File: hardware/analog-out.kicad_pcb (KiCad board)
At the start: 2 copper layers, 30 x 35 mm, 30 parts, among them P1 CON-SENSOR, P2 CONN_5, U1 M24C64, U2 MCP4725A0, U3 TLV272IS, U4 DRILL, U5 DRILL, U6 DRILL, U7 DRILL

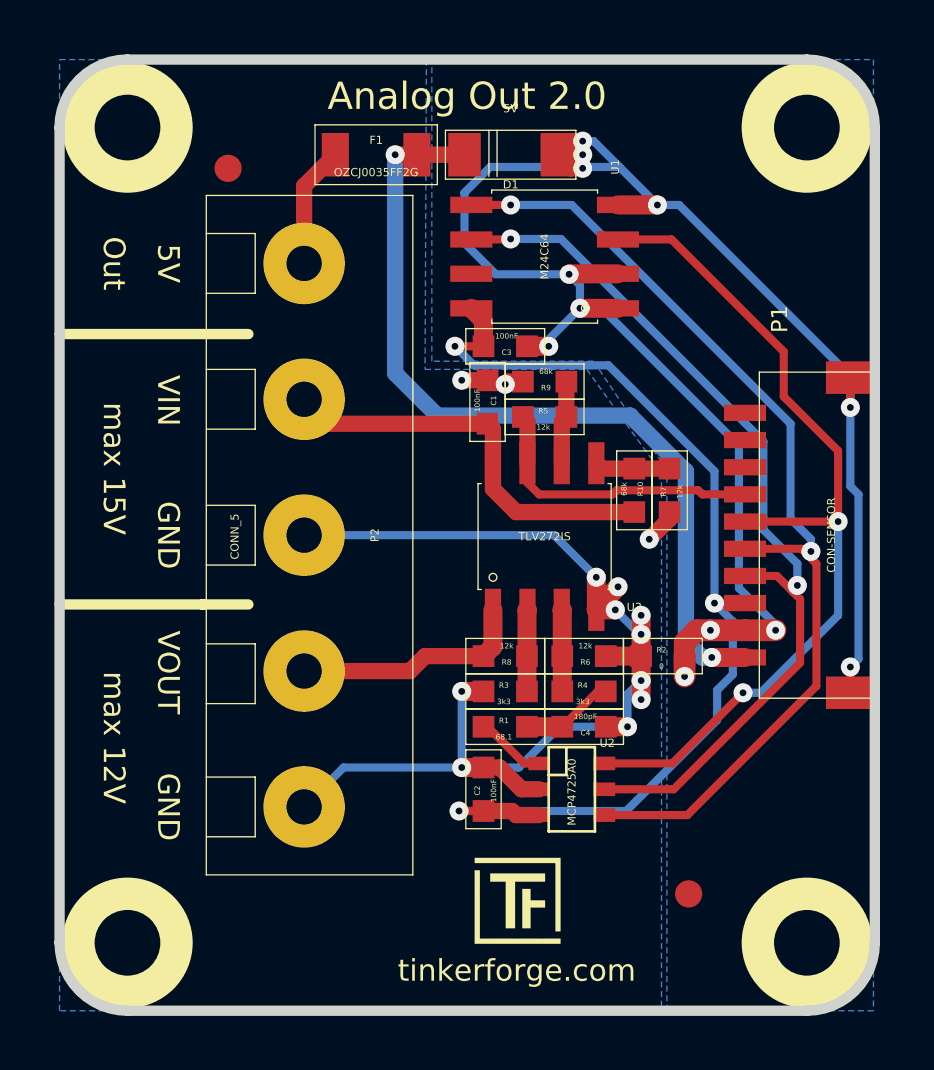
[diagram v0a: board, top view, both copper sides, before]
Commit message: use tinkerforge symbols instead of kicad symbols
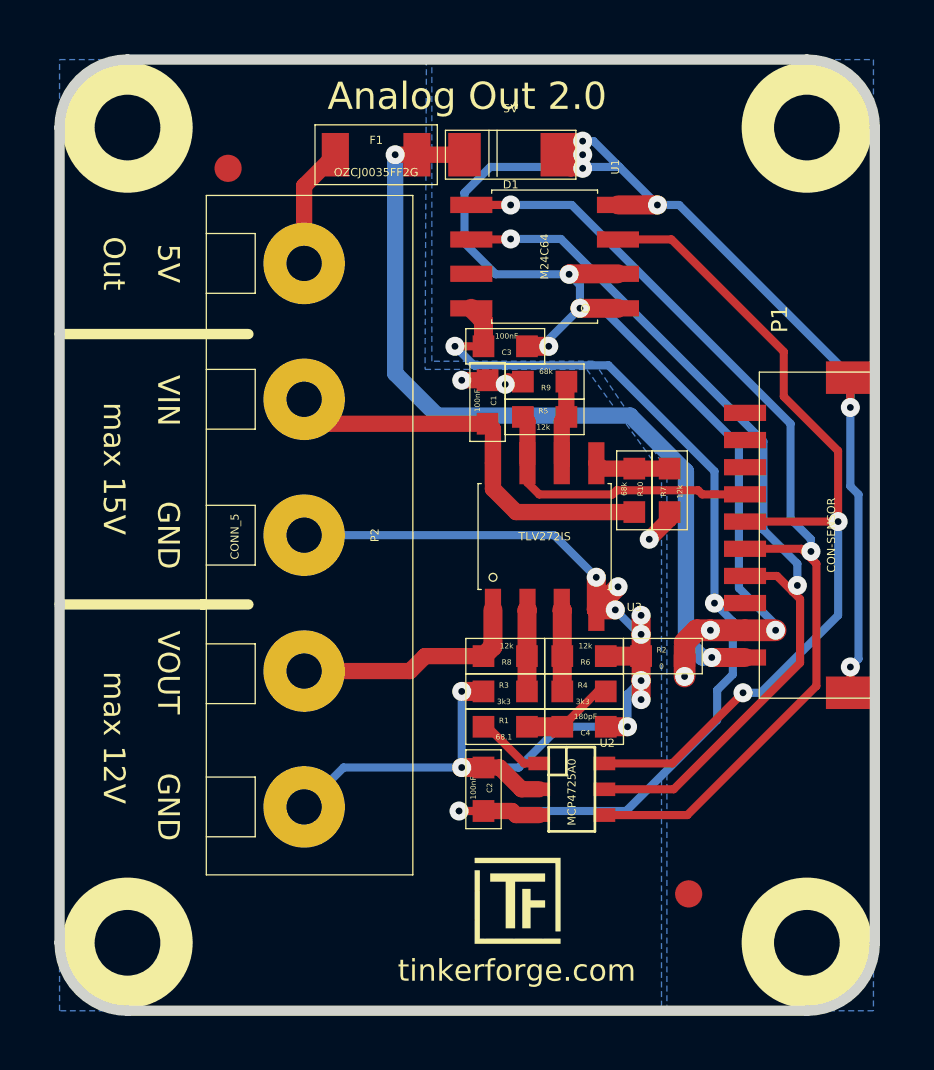
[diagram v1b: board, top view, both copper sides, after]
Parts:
- turned C2 to 90 degrees
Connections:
- C2 pad 1: AGND -> 3V3
- C2 pad 2: 3V3 -> AGND
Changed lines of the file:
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@@
-(kicad_pcb (version 4) (host pcbnew "(2015-03-18 BZR 5525)-product")
+(kicad_pcb (version 4) (host pcbnew 4.0.7-e0-6372~58~ubuntu16.10.1)
   (general
     (links 50)
     (no_connects 0)
-    (area 137.195139 81.720139 281.746642 165.290183)
+    (area 137.858499 82.381719 168.240721 117.765501)
     (thickness 1.6002)
     (drawings 22)
@@
   )
   (module kicad-libraries:0603 (layer Vorderseite)
-    (at 153.65 109.425 270)
+    (at 153.65 109.425 90)
     (attr smd)
-    (fp_text reference C2 (at 0.05 0.225 270) (layer F.SilkS)
+    (fp_text reference C2 (at 0.05 0.225 90) (layer F.SilkS)
       (effects (font (size 0.2 0.2) (thickness 0.05)))
     )
-    (fp_text value 100nF (at 0.05 -0.375 270) (layer F.SilkS)
+    (fp_text value 100nF (at 0.05 -0.375 90) (layer F.SilkS)
       (effects (font (size 0.2 0.2) (thickness 0.05)))
     )
@@
     (fp_line (start 1.45034 0.65024) (end -1.45034 0.65024) (layer F.SilkS) (width 0.001))
     (fp_line (start -1.45034 0.65024) (end -1.45034 -0.65024) (layer F.SilkS) (width 0.001))
-    (pad 1 smd rect (at -0.8001 0 270) (size 0.8001 0.8001) (layers Vorderseite F.Paste F.Mask)
-      (net 6 AGND))
-    (pad 2 smd rect (at 0.8001 0 270) (size 0.8001 0.8001) (layers Vorderseite F.Paste F.Mask)
+    (pad 1 smd rect (at -0.8001 0 90) (size 0.8001 0.8001) (layers Vorderseite F.Paste F.Mask)
       (net 7 3V3))
+    (pad 2 smd rect (at 0.8001 0 90) (size 0.8001 0.8001) (layers Vorderseite F.Paste F.Mask)
+      (net 6 AGND))
   )
   (module kicad-libraries:0603 (layer Vorderseite)
@@
   (via (at 157.3 86.575) (size 0.70104) (layers Vorderseite Rückseite) (net 2))
   (segment (start 156.34926 86.075) (end 156.84926 85.575) (width 0.59944) (layer Vorderseite) (net 2))
+  (segment (start 153.9 86.525) (end 157.3 86.525) (width 0.29972) (layer Rückseite) (net 2))
+  (segment (start 157.3 86.525) (end 158.65 86.525) (width 0.29972) (layer Rückseite) (net 2))
+  (segment (start 158.65 86.525) (end 160.05 87.925) (width 0.29972) (layer Rückseite) (net 2))
+  (via (at 160.05 87.925) (size 0.70104) (layers Vorderseite Rückseite) (net 2))
+  (segment (start 160.85 87.925) (end 167.15 94.225) (width 0.29972) (layer Rückseite) (net 2))
+  (segment (start 167.15 94.225) (end 167.15 95.375) (width 0.29972) (layer Rückseite) (net 2))
+  (via (at 167.15 95.375) (size 0.70104) (layers Vorderseite Rückseite) (net 2))
+  (segment (start 167.15 95.375) (end 167.15084 95.37416) (width 0.29972) (layer Vorderseite) (net 2))
+  (segment (start 160.05 87.925) (end 160.85 87.925) (width 0.29972) (layer Rückseite) (net 2))
+  (segment (start 167.15 98.275) (end 167.45 98.575) (width 0.29972) (layer Rückseite) (net 2))
+  (segment (start 167.45 98.575) (end 167.45 104.625) (width 0.29972) (layer Rückseite) (net 2))
+  (segment (start 167.45 104.625) (end 167.15 104.925) (width 0.29972) (layer Rückseite) (net 2))
+  (via (at 167.15 104.925) (size 0.70104) (layers Vorderseite Rückseite) (net 2))
+  (segment (start 167.15 104.925) (end 167.15084 104.92584) (width 0.29972) (layer Vorderseite) (net 2))
+  (segment (start 167.15 95.375) (end 167.15 98.275) (width 0.29972) (layer Rückseite) (net 2))
+  (via (at 157.3 86.075) (size 0.70104) (layers Vorderseite Rückseite) (net 2))
+  (segment (start 156.34926 86.075) (end 157.3 86.075) (width 0.7) (layer Vorderseite) (net 2))
   (segment (start 161.0501 104.0249) (end 161.0501 104.525) (width 0.7) (layer Vorderseite) (net 2))
   (segment (start 161.0501 105.2749) (end 161.05 105.275) (width 0.7) (layer Vorderseite) (net 2))
@@
   (segment (start 152.95 89.325) (end 152.95 87.475) (width 0.29972) (layer Rückseite) (net 2))
   (segment (start 152.95 87.475) (end 153.9 86.525) (width 0.29972) (layer Rückseite) (net 2))
-  (segment (start 153.9 86.525) (end 157.3 86.525) (width 0.29972) (layer Rückseite) (net 2))
-  (segment (start 157.3 86.525) (end 158.65 86.525) (width 0.29972) (layer Rückseite) (net 2))
-  (segment (start 158.65 86.525) (end 160.05 87.925) (width 0.29972) (layer Rückseite) (net 2))
   (segment (start 160.04754 87.92254) (end 158.59748 87.92254) (width 0.7) (layer Vorderseite) (net 2))
-  (via (at 160.05 87.925) (size 0.70104) (layers Vorderseite Rückseite) (net 2))
   (segment (start 160.04754 87.92254) (end 160.05 87.925) (width 0.7) (layer Vorderseite) (net 2))
   (segment (start 156.8 90.475) (end 154.1 90.475) (width 0.29972) (layer Rückseite) (net 2))
-  (segment (start 160.85 87.925) (end 167.15 94.225) (width 0.29972) (layer Rückseite) (net 2))
-  (segment (start 167.15 94.225) (end 167.15 95.375) (width 0.29972) (layer Rückseite) (net 2))
-  (via (at 167.15 95.375) (size 0.70104) (layers Vorderseite Rückseite) (net 2))
-  (segment (start 167.15 95.375) (end 167.15084 95.37416) (width 0.29972) (layer Vorderseite) (net 2))
   (segment (start 167.15084 95.37416) (end 167.15084 94.27618) (width 0.29972) (layer Vorderseite) (net 2))
-  (segment (start 160.05 87.925) (end 160.85 87.925) (width 0.29972) (layer Rückseite) (net 2))
-  (segment (start 167.15 98.275) (end 167.45 98.575) (width 0.29972) (layer Rückseite) (net 2))
-  (segment (start 167.45 98.575) (end 167.45 104.625) (width 0.29972) (layer Rückseite) (net 2))
-  (segment (start 167.45 104.625) (end 167.15 104.925) (width 0.29972) (layer Rückseite) (net 2))
-  (via (at 167.15 104.925) (size 0.70104) (layers Vorderseite Rückseite) (net 2))
-  (segment (start 167.15 104.925) (end 167.15084 104.92584) (width 0.29972) (layer Vorderseite) (net 2))
   (segment (start 167.15084 104.92584) (end 167.15084 105.87382) (width 0.29972) (layer Vorderseite) (net 2))
-  (segment (start 167.15 95.375) (end 167.15 98.275) (width 0.29972) (layer Rückseite) (net 2))
   (segment (start 164.4 103.375) (end 163.05 102.025) (width 0.29972) (layer Rückseite) (net 2))
   (segment (start 163.05 102.025) (end 163.05 96.775) (width 0.29972) (layer Rückseite) (net 2))
@@
   (segment (start 164.39988 103.57512) (end 164.4 103.575) (width 0.7) (layer Vorderseite) (net 2))
   (segment (start 164.4 103.575) (end 164.4 103.375) (width 0.29972) (layer Rückseite) (net 2))
-  (via (at 157.3 86.075) (size 0.70104) (layers Vorderseite Rückseite) (net 2))
-  (segment (start 156.34926 86.075) (end 157.3 86.075) (width 0.7) (layer Vorderseite) (net 2))
   (segment (start 165.025 102.15) (end 165.3 102.425) (width 0.29972) (layer Vorderseite) (net 3))
   (segment (start 164.45114 101.57614) (end 165.025 102.15) (width 0.29972) (layer Vorderseite) (net 3))
@@
   (segment (start 152.85 105.825) (end 153.6499 105.825) (width 0.7) (layer Vorderseite) (net 6))
   (segment (start 155.05 109.425) (end 154.2499 108.6249) (width 0.59944) (layer Vorderseite) (net 6))
-  (segment (start 154.2499 108.6249) (end 153.65 108.6249) (width 0.59944) (layer Vorderseite) (net 6))
   (segment (start 155.70112 109.425) (end 155.05 109.425) (width 0.59944) (layer Vorderseite) (net 6))
   (via (at 158.6 101.975) (size 0.70104) (layers Vorderseite Rückseite) (net 6))
@@
   (segment (start 157.80246 102.82248) (end 157.80246 102.77254) (width 0.7) (layer Vorderseite) (net 6))
   (via (at 152.85 105.825) (size 0.70104) (layers Vorderseite Rückseite) (net 6))
-  (segment (start 153.65 108.6249) (end 152.8501 108.6249) (width 0.7) (layer Vorderseite) (net 6))
   (via (at 152.85 108.625) (size 0.70104) (layers Vorderseite Rückseite) (net 6))
-  (segment (start 152.8501 108.6249) (end 152.85 108.625) (width 0.7) (layer Vorderseite) (net 6))
   (segment (start 152.85 108.625) (end 152.85 105.825) (width 0.29972) (layer Rückseite) (net 6))
   (segment (start 156.45 107.125) (end 154.95 108.625) (width 0.29972) (layer Rückseite) (net 6))
@@
   (segment (start 160.5 99.475) (end 159.75 100.225) (width 0.59944) (layer Vorderseite) (net 6))
   (segment (start 160.5 99.2251) (end 160.5 99.475) (width 0.59944) (layer Vorderseite) (net 6))
-  (segment (start 154.84996 110.37496) (end 154.7001 110.2251) (width 0.59944) (layer Vorderseite) (net 7))
+  (segment (start 152.8501 108.6249) (end 152.85 108.625) (width 0.7) (layer Vorderseite) (net 6))
+  (segment (start 154.2499 108.6249) (end 153.65 108.6249) (width 0.59944) (layer Vorderseite) (net 6))
+  (segment (start 153.65 108.6249) (end 152.8501 108.6249) (width 0.7) (layer Vorderseite) (net 6))
   (segment (start 154.7001 110.2251) (end 153.65 110.2251) (width 0.59944) (layer Vorderseite) (net 7))
-  (segment (start 155.70112 110.37496) (end 154.84996 110.37496) (width 0.59944) (layer Vorderseite) (net 7))
   (segment (start 152.7501 110.2251) (end 152.75 110.225) (width 0.29972) (layer Vorderseite) (net 7))
   (via (at 152.75 110.225) (size 0.70104) (layers Vorderseite Rückseite) (net 7))
@@
   (segment (start 152.75 110.225) (end 158.9 110.225) (width 0.29972) (layer Rückseite) (net 7))
   (segment (start 153.65 110.2251) (end 152.7501 110.2251) (width 0.29972) (layer Vorderseite) (net 7))
-  (segment (start 153.6499 92.17484) (end 153.20252 91.72746) (width 0.7) (layer Vorderseite) (net 7))
-  (segment (start 153.6499 93.125) (end 153.6499 92.17484) (width 0.7) (layer Vorderseite) (net 7))
   (segment (start 162.825 105.2) (end 162.25 105.775) (width 0.29972) (layer Rückseite) (net 7))
   (segment (start 162.25 105.775) (end 162.25 106.875) (width 0.29972) (layer Rückseite) (net 7))
   (segment (start 162.25 106.875) (end 158.9 110.225) (width 0.29972) (layer Rückseite) (net 7))
+  (segment (start 154.84996 110.37496) (end 154.7001 110.2251) (width 0.59944) (layer Vorderseite) (net 7))
+  (segment (start 155.70112 110.37496) (end 154.84996 110.37496) (width 0.59944) (layer Vorderseite) (net 7))
+  (segment (start 153.6499 92.17484) (end 153.20252 91.72746) (width 0.7) (layer Vorderseite) (net 7))
+  (segment (start 153.6499 93.125) (end 153.6499 92.17484) (width 0.7) (layer Vorderseite) (net 7))
   (via (at 162.15 102.575) (size 0.70104) (layers Vorderseite Rückseite) (net 7))
   (segment (start 163.2748 102.57436) (end 162.15064 102.57436) (width 0.29972) (layer Vorderseite) (net 7))

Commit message: Add 3d information (final)
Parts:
- C1, C2, C3, C4: footprint kicad-libraries:0603 -> kicad-libraries:C0603
- F1: footprint kicad-libraries:1206 -> kicad-libraries:F1206
- Fiducial_Mark (x2): footprint Fiducial_Mark -> kicad-libraries:Fiducial_Mark
- R1, R10, R2, R3, R4, R5, R6, R7, R8, R9: footprint kicad-libraries:0603 -> kicad-libraries:R0603
- Ref**: footprint Logo_31x31 -> kicad-libraries:Logo_31x31
- VAL: footprint CE_5mm -> kicad-libraries:CE_5mm
- VAL: footprint WEEE_7mm -> kicad-libraries:WEEE_7mm
- turned VAL to 180 degrees
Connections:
- P1 pad 10: (no net) -> Net-(P1-Pad10)
- P1 pad 8: (no net) -> Net-(P1-Pad8)
- P1 pad 9: (no net) -> Net-(P1-Pad9)
- U1 pad 7: (no net) -> Net-(U1-Pad7)
